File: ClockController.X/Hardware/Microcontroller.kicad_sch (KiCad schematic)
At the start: 3 parts, among them U1 PIC16F15224-I/SL

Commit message: Updated most footprints
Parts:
- C2: footprint Clock Controller:CAP_0805 -> Capacitor_SMD:C_0805_2012Metric
- ICSP0: footprint Clock Controller:RHDRRA5W60P0X254_1X5_1320X850X274P -> Connector_PinSocket_2.54mm:PinSocket_1x05_P2.54mm_Horizontal
- U1: footprint Clock Controller:SOIC14P127_869X599X175L84X42N -> Package_SO:SOIC-14_3.9x8.7mm_P1.27mm
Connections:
- net ICSPCLK: now also ICSP0.1; no longer ICSP0.5
- net ICSPDAT: now also ICSP0.2; no longer ICSP0.4
- net V5V: now also ICSP0.4; no longer ICSP0.2
- net ~{MCLR}: now also ICSP0.5; no longer ICSP0.1
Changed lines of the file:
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@@
+	(wire
+		(pts
+			(xy 135.89 77.47) (xy 138.43 77.47)
+		)
+		(stroke
+			(width 0)
+			(type default)
+		)
+	)
 	(wire
 		(pts
@@
 	(wire
 		(pts
-			(xy 129.54 82.55) (xy 128.27 82.55)
-		)
-		(stroke
-			(width 0.25)
-			(type solid)
-		)
-	)
-	(wire
-		(pts
 			(xy 78.74 107.95) (xy 80.01 107.95)
 		)
@@
 	(wire
 		(pts
+			(xy 135.89 80.01) (xy 138.43 80.01)
+		)
+		(stroke
+			(width 0)
+			(type default)
+		)
+	)
+	(wire
+		(pts
 			(xy 209.55 102.87) (xy 207.01 102.87)
 		)
@@
 	(wire
 		(pts
-			(xy 138.43 87.63) (xy 137.16 87.63)
-		)
-		(stroke
-			(width 0)
-			(type default)
-		)
-	)
-	(wire
-		(pts
 			(xy 78.74 118.11) (xy 80.01 118.11)
 		)
@@
 	(wire
 		(pts
+			(xy 135.89 87.63) (xy 138.43 87.63)
+		)
+		(stroke
+			(width 0)
+			(type default)
+		)
+	)
+	(wire
+		(pts
+			(xy 130.81 82.55) (xy 138.43 82.55)
+		)
+		(stroke
+			(width 0)
+			(type default)
+		)
+	)
+	(wire
+		(pts
 			(xy 205.74 130.81) (xy 147.32 130.81)
 		)
@@
 	(wire
 		(pts
-			(xy 137.16 80.01) (xy 138.43 80.01)
-		)
-		(stroke
-			(width 0)
-			(type default)
-		)
-	)
-	(wire
-		(pts
 			(xy 78.74 120.65) (xy 80.01 120.65)
 		)
@@
 	(wire
 		(pts
-			(xy 137.16 77.47) (xy 138.43 77.47)
-		)
-		(stroke
-			(width 0)
-			(type default)
-		)
-	)
-	(wire
-		(pts
-			(xy 129.54 82.55) (xy 138.43 82.55)
-		)
-		(stroke
-			(width 0)
-			(type default)
-		)
-	)
-	(wire
-		(pts
 			(xy 209.55 102.87) (xy 205.74 102.87)
 		)
@@
 			(width 0.25)
 			(type solid)
+		)
+	)
+	(wire
+		(pts
+			(xy 135.89 85.09) (xy 138.43 85.09)
+		)
+		(stroke
+			(width 0)
+			(type default)
 		)
 	)
@@
 	)
 	(label "ICSPDAT"
-		(at 137.16 80.01 180)
+		(at 135.89 85.09 180)
 		(fields_autoplaced yes)
 		(effects
@@
 	)
 	(label "~{MCLR}"
-		(at 137.16 87.63 180)
+		(at 135.89 77.47 180)
 		(fields_autoplaced yes)
 		(effects
@@
 	)
 	(label "ICSPCLK"
-		(at 137.16 77.47 180)
+		(at 135.89 87.63 180)
 		(fields_autoplaced yes)
 		(effects
@@
 	(global_label "V5V"
 		(shape bidirectional)
-		(at 138.43 85.09 180)
+		(at 135.89 80.01 180)
 		(fields_autoplaced yes)
 		(effects
@@
 		)
 		(property "Intersheetrefs" "${INTERSHEET_REFS}"
-			(at 132.4437 85.09 0)
+			(at 129.9037 80.01 0)
 			(effects
 				(font
@@
 			)
 		)
-		(property "Footprint" "Clock Controller:SOIC14P127_869X599X175L84X42N"
+		(property "Footprint" "Package_SO:SOIC-14_3.9x8.7mm_P1.27mm"
 			(at 143.51 110.49 0)
 			(effects
@@
 	(symbol
 		(lib_id "Clock Controller-eagle-import:GND_DIGITAL")
-		(at 124.46 82.55 270)
+		(at 127 82.55 270)
 		(unit 1)
 		(exclude_from_sim no)
@@
 		(dnp no)
 		(property "Reference" "#NetPort04"
-			(at 124.46 82.55 0)
+			(at 127 82.55 0)
 			(effects
 				(font
@@
 		)
 		(property "Value" "GND_DIGITAL"
-			(at 124.46 82.55 0)
+			(at 127 82.55 0)
 			(effects
 				(font
@@
 		)
 		(property "Footprint" ""
-			(at 124.46 82.55 0)
+			(at 127 82.55 0)
 			(effects
 				(font
@@
 		)
 		(property "Datasheet" ""
-			(at 124.46 82.55 0)
+			(at 127 82.55 0)
 			(effects
 				(font
@@
 		)
 		(property "Description" ""
-			(at 124.46 82.55 0)
+			(at 127 82.55 0)
 			(effects
 				(font
@@
 			)
 		)
-		(property "Footprint" "Clock Controller:RHDRRA5W60P0X254_1X5_1320X850X274P"
+		(property "Footprint" "Connector_PinSocket_2.54mm:PinSocket_1x05_P2.54mm_Horizontal"
 			(at 138.43 87.63 0)
 			(effects
@@
 			)
 		)
-		(property "Footprint" "Clock Controller:CAP_0805"
+		(property "Footprint" "Capacitor_SMD:C_0805_2012Metric"
 			(at 143.51 130.81 0)
 			(effects

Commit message: Replacing many thin traces with poured zones.
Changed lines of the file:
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@@
 (kicad_sch
-	(version 20231120)
+	(version 20250114)
 	(generator "eeschema")
-	(generator_version "8.0")
+	(generator_version "9.0")
 	(paper "A4")
+	(text "PIC16F15224-I/SL"
+		(exclude_from_sim no)
+		(at 203.2 97.79 0)
+		(effects
+			(font
+				(size 1.48 1.48)
+			)
+			(justify left bottom)
+		)
+	)
+	(text "C2"
+		(exclude_from_sim no)
+		(at 142.218 128.899 0)
+		(effects
+			(font
+				(size 1.48 1.48)
+			)
+			(justify left bottom)
+		)
+	)
+	(text "ICSP"
+		(exclude_from_sim no)
+		(at 151.384 74.168 0)
+		(effects
+			(font
+				(size 1.48 1.48)
+			)
+			(justify right bottom)
+		)
+	)
+	(text "U1"
+		(exclude_from_sim no)
+		(at 142.581 123.19 0)
+		(effects
+			(font
+				(size 1.48 1.48)
+			)
+			(justify left top)
+		)
+	)
 	(junction
 		(at 68.58 130.81)
@@
 		)
 	)
-	(text "PIC16F15224-I/SL"
-		(exclude_from_sim no)
-		(at 203.2 97.79 0)
-		(effects
-			(font
-				(size 1.48 1.48)
-			)
-			(justify left bottom)
-		)
-	)
-	(text "C2"
-		(exclude_from_sim no)
-		(at 142.218 128.899 0)
-		(effects
-			(font
-				(size 1.48 1.48)
-			)
-			(justify left bottom)
-		)
-	)
-	(text "ICSP"
-		(exclude_from_sim no)
-		(at 151.384 74.168 0)
-		(effects
-			(font
-				(size 1.48 1.48)
-			)
-			(justify right bottom)
-		)
-	)
-	(text "U1"
-		(exclude_from_sim no)
-		(at 142.581 123.19 0)
-		(effects
-			(font
-				(size 1.48 1.48)
-			)
-			(justify left top)
-		)
-	)
 	(label "~{MCLR}"
 		(at 209.55 105.41 0)
-		(fields_autoplaced yes)
 		(effects
 			(font
@@
 	(label "ICSPDAT"
 		(at 135.89 85.09 180)
-		(fields_autoplaced yes)
 		(effects
 			(font
@@
 	(label "~{MCLR}"
 		(at 135.89 77.47 180)
-		(fields_autoplaced yes)
 		(effects
 			(font
@@
 	(label "ICSPCLK"
 		(at 135.89 87.63 180)
-		(fields_autoplaced yes)
 		(effects
 			(font
@@
 	(label "ICSPCLK"
 		(at 209.55 110.49 0)
-		(fields_autoplaced yes)
 		(effects
 			(font
@@
 	(label "ICSPDAT"
 		(at 209.55 113.03 0)
-		(fields_autoplaced yes)
-		(effects
-			(font
+		(effects
+			(font

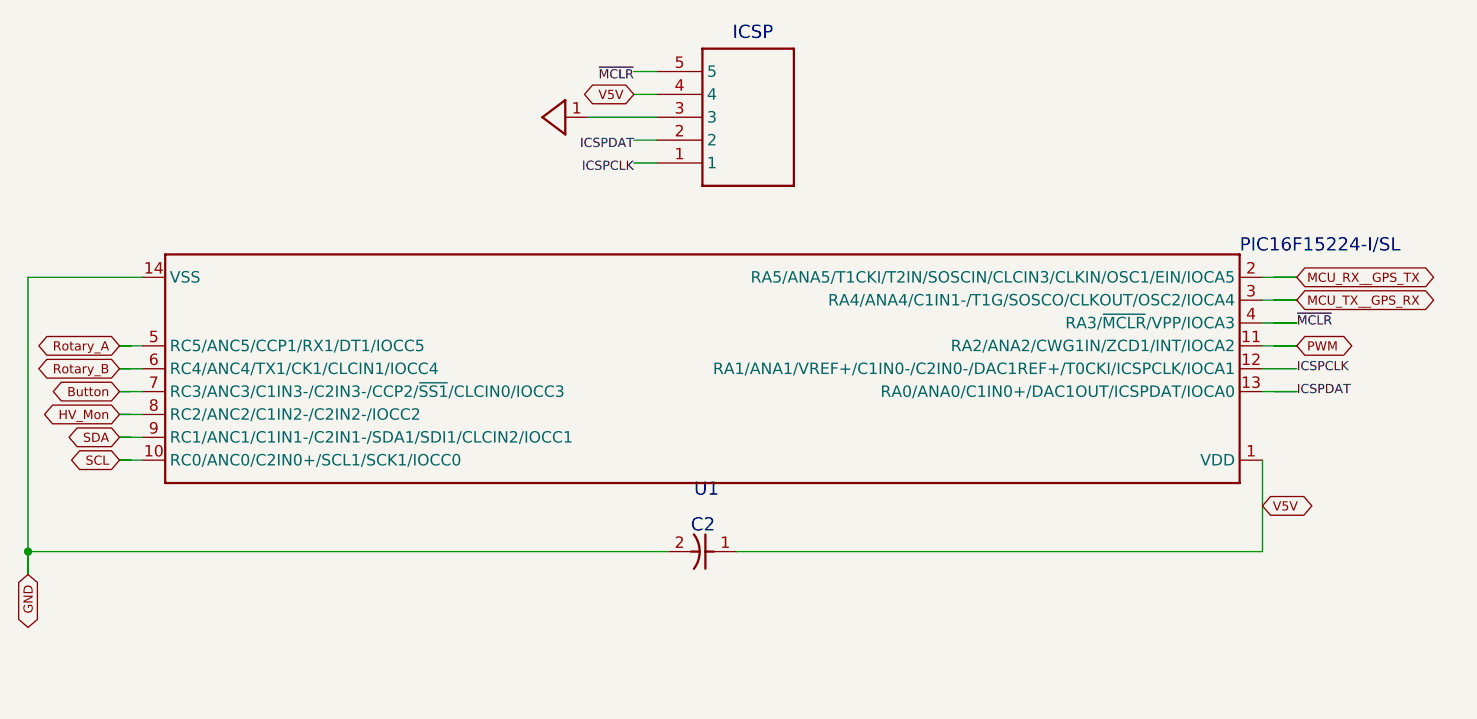
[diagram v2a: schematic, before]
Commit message: Replace the imported objects with native kicad equivalents
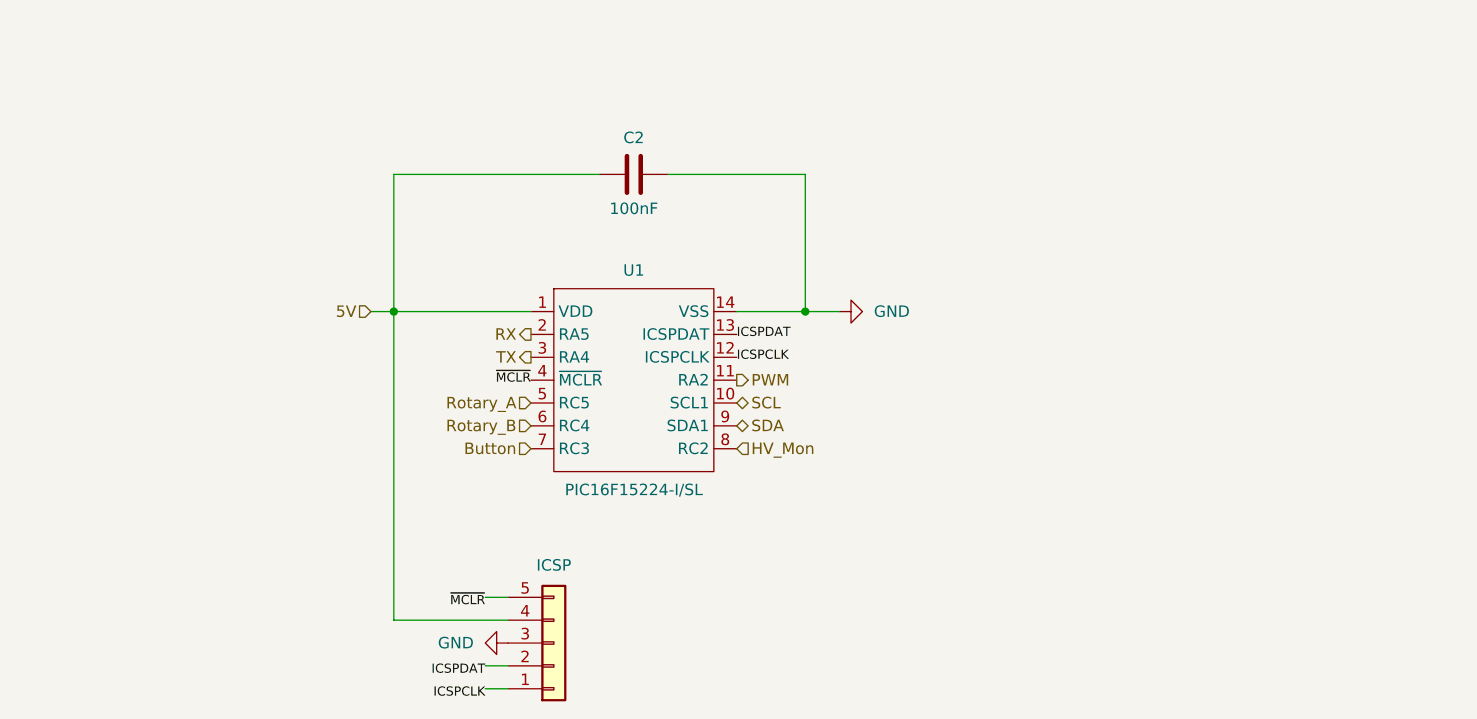
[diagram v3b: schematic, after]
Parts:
- C2: symbol Clock Controller-eagle-import:CAP_0805 -> Device:C
- ICSP0: value PPPC051LGBN-RC -> ICSP; symbol Clock Controller-eagle-import:PPPC051LGBN-RC -> Connector_Generic:Conn_01x05
- U1: symbol Clock Controller-eagle-import:PIC16F15224-I/SL -> MCU_Microchip_PIC16_:PIC16F15224-I/SL
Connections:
- net GND_DIGITAL is gone; now on net GND: ICSP0.3 (Pin_3)
- net MCU_RX__GPS_TX renamed RX
- net MCU_TX__GPS_RX renamed TX
- net V5V renamed 5V
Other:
- note removed: "C2"
- note removed: "ICSP"
- note removed: "PIC16F15224-I/SL"
- note removed: "U1"

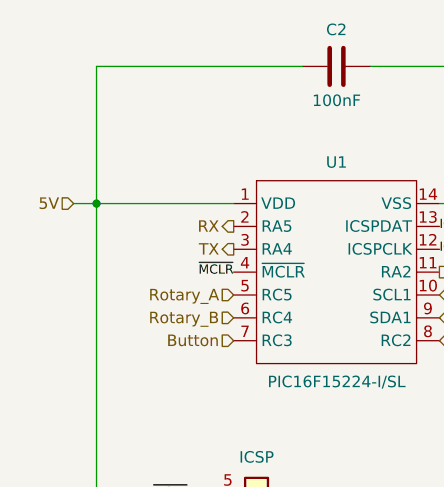
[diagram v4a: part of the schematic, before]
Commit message: Converting to single board layout
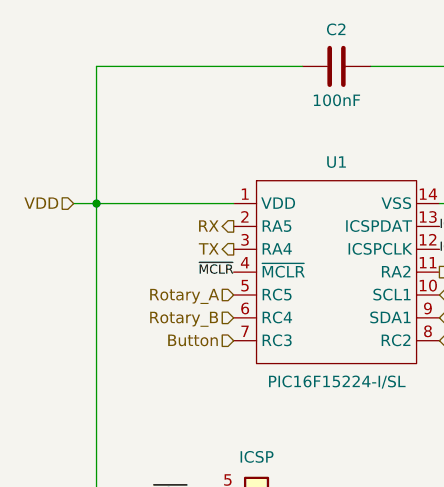
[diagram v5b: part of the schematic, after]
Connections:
- net 5V renamed VDD
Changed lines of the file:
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@@
 	(generator "eeschema")
 	(generator_version "9.0")
-	(paper "A4")
+	(paper "USLetter")
 	(junction
 		(at 154.94 104.14)
@@
 		)
 	)
-	(hierarchical_label "5V"
+	(hierarchical_label "VDD"
 		(shape input)
 		(at 106.68 104.14 180)
